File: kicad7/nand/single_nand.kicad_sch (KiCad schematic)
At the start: 14 parts, among them U1 TL074

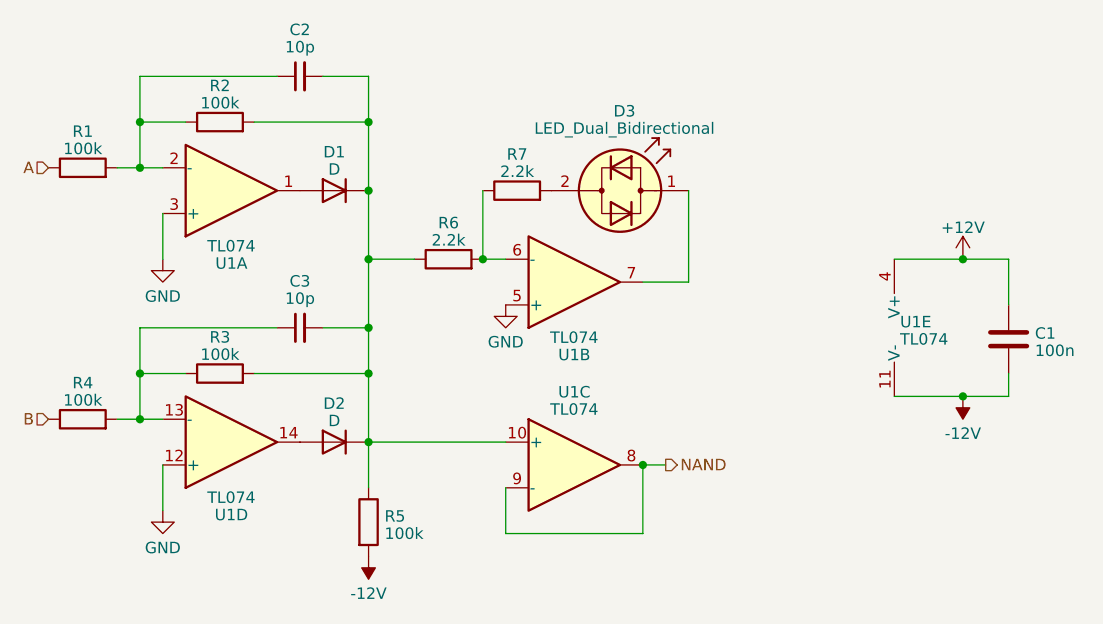
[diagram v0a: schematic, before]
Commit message: alt nand submodule layout. looking better but a lot of jumpers
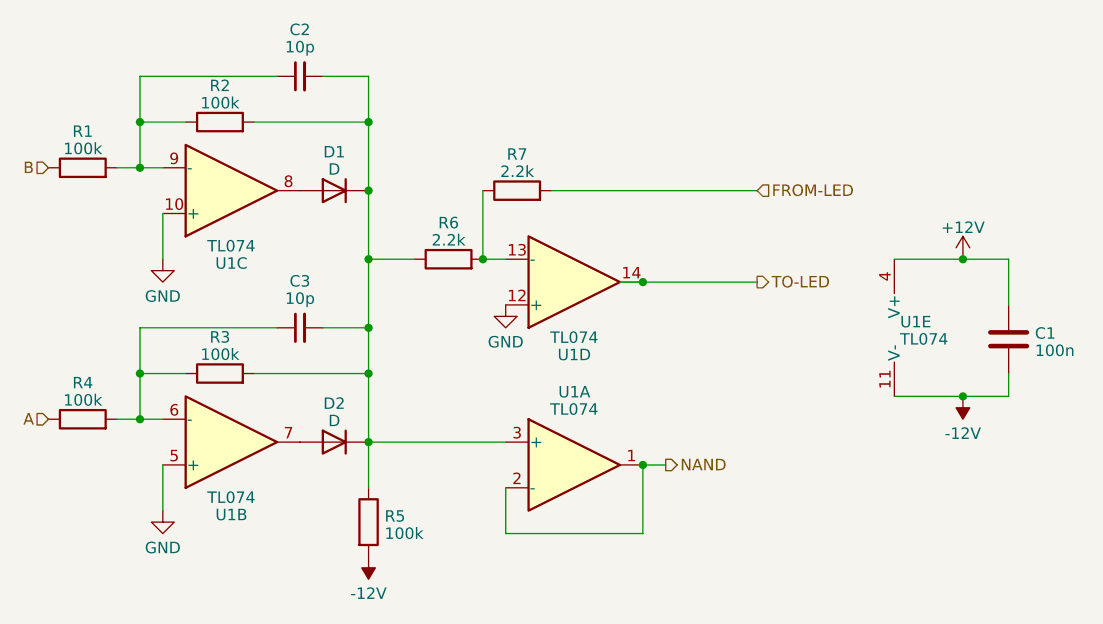
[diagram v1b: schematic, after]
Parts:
- removed D3: LED_Dual_Bidirectional, LED_THT:LED_D3.0mm, symbol Device:LED_Dual_Bidirectional
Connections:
- net A: now also R4.1; no longer R1.1
- net B: now also R1.1; no longer R4.1
- net GND: now also U1.10 (+), U1.12 (+), U1.5 (+); no longer U1.12 (+), U1.3 (+), U1.5 (+)
- net NAND: now also U1.1, U1.2 (-); no longer U1.8, U1.9 (-)
- net FROM-LED: now reaches R7.2
- net at C2.1, R1.2, R2.1: now also U1.9 (-); no longer U1.2 (-)
- net at C3.1, R3.1, R4.2: now also U1.6 (-); no longer U1.13 (-)
- net at D2.2 (A): now also U1.7; no longer U1.14
- net at R6.2, R7.1: now also U1.13 (-); no longer U1.6 (-)
- net at C2.2, C3.2, D1.1 (K)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: now also U1.3 (+); no longer U1.10 (+)
- net at D1.2 (A): now also U1.8; no longer U1.1
- new net TO-LED: U1.14
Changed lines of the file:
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@@
 (kicad_sch (version 20230121) (generator eeschema)
   (paper "A4")
+  (junction (at 58.42 33.02) (diameter 0) (color 0 0 0 0)
+  )
   (junction (at 58.42 38.1) (diameter 0) (color 0 0 0 0)
   )
-  (junction (at 58.42 33.02) (diameter 0) (color 0 0 0 0)
-  )
   (junction (at 114.3 71.12) (diameter 0) (color 0 0 0 0)
   )
@@
   (junction (at 83.82 55.88) (diameter 0) (color 0 0 0 0)
   )
+  (junction (at 114.3 50.8) (diameter 0) (color 0 0 0 0)
+  )
   (junction (at 83.82 33.02) (diameter 0) (color 0 0 0 0)
   )
@@
     (stroke (width 0) (type default))
   )
+  (wire (pts (xy 99.06 78.74) (xy 99.06 73.66))
+    (stroke (width 0) (type default))
+  )
+  (wire (pts (xy 83.82 48.26) (xy 83.82 55.88))
+    (stroke (width 0) (type default))
+  )
+  (wire (pts (xy 104.14 40.64) (xy 127 40.64))
+    (stroke (width 0) (type default))
+  )
+  (wire (pts (xy 58.42 38.1) (xy 60.96 38.1))
+    (stroke (width 0) (type default))
+  )
+  (wire (pts (xy 83.82 60.96) (xy 83.82 68.58))
+    (stroke (width 0) (type default))
+  )
+  (wire (pts (xy 78.74 55.88) (xy 83.82 55.88))
+    (stroke (width 0) (type default))
+  )
+  (wire (pts (xy 55.88 66.04) (xy 58.42 66.04))
+    (stroke (width 0) (type default))
+  )
+  (wire (pts (xy 71.12 60.96) (xy 83.82 60.96))
+    (stroke (width 0) (type default))
+  )
+  (wire (pts (xy 83.82 68.58) (xy 83.82 73.66))
+    (stroke (width 0) (type default))
+  )
+  (wire (pts (xy 154.94 63.5) (xy 154.94 60.96))
+    (stroke (width 0) (type default))
+  )
+  (wire (pts (xy 78.74 27.94) (xy 83.82 27.94))
+    (stroke (width 0) (type default))
+  )
+  (wire (pts (xy 111.76 50.8) (xy 114.3 50.8))
+    (stroke (width 0) (type default))
+  )
+  (wire (pts (xy 96.52 48.26) (xy 99.06 48.26))
+    (stroke (width 0) (type default))
+  )
+  (wire (pts (xy 83.82 68.58) (xy 99.06 68.58))
+    (stroke (width 0) (type default))
+  )
+  (wire (pts (xy 73.66 55.88) (xy 58.42 55.88))
+    (stroke (width 0) (type default))
+  )
+  (wire (pts (xy 114.3 78.74) (xy 99.06 78.74))
+    (stroke (width 0) (type default))
+  )
+  (wire (pts (xy 58.42 27.94) (xy 58.42 33.02))
+    (stroke (width 0) (type default))
+  )
+  (wire (pts (xy 71.12 33.02) (xy 83.82 33.02))
+    (stroke (width 0) (type default))
+  )
+  (wire (pts (xy 83.82 55.88) (xy 83.82 60.96))
+    (stroke (width 0) (type default))
+  )
+  (wire (pts (xy 83.82 48.26) (xy 88.9 48.26))
+    (stroke (width 0) (type default))
+  )
+  (wire (pts (xy 58.42 66.04) (xy 60.96 66.04))
+    (stroke (width 0) (type default))
+  )
+  (wire (pts (xy 58.42 60.96) (xy 63.5 60.96))
+    (stroke (width 0) (type default))
+  )
+  (wire (pts (xy 58.42 55.88) (xy 58.42 60.96))
+    (stroke (width 0) (type default))
+  )
+  (wire (pts (xy 96.52 40.64) (xy 96.52 48.26))
+    (stroke (width 0) (type default))
+  )
+  (wire (pts (xy 60.96 43.18) (xy 60.96 48.26))
+    (stroke (width 0) (type default))
+  )
+  (wire (pts (xy 149.86 63.5) (xy 154.94 63.5))
+    (stroke (width 0) (type default))
+  )
+  (wire (pts (xy 114.3 71.12) (xy 114.3 78.74))
+    (stroke (width 0) (type default))
+  )
   (wire (pts (xy 55.88 38.1) (xy 58.42 38.1))
     (stroke (width 0) (type default))
   )
-  (wire (pts (xy 99.06 78.74) (xy 99.06 73.66))
-    (stroke (width 0) (type default))
-  )
-  (wire (pts (xy 83.82 48.26) (xy 83.82 55.88))
-    (stroke (width 0) (type default))
-  )
-  (wire (pts (xy 58.42 38.1) (xy 60.96 38.1))
-    (stroke (width 0) (type default))
-  )
-  (wire (pts (xy 83.82 60.96) (xy 83.82 68.58))
-    (stroke (width 0) (type default))
-  )
-  (wire (pts (xy 78.74 55.88) (xy 83.82 55.88))
-    (stroke (width 0) (type default))
-  )
-  (wire (pts (xy 55.88 66.04) (xy 58.42 66.04))
-    (stroke (width 0) (type default))
-  )
-  (wire (pts (xy 71.12 60.96) (xy 83.82 60.96))
-    (stroke (width 0) (type default))
-  )
-  (wire (pts (xy 83.82 68.58) (xy 83.82 73.66))
-    (stroke (width 0) (type default))
-  )
-  (wire (pts (xy 154.94 63.5) (xy 154.94 60.96))
-    (stroke (width 0) (type default))
-  )
-  (wire (pts (xy 78.74 27.94) (xy 83.82 27.94))
-    (stroke (width 0) (type default))
-  )
-  (wire (pts (xy 96.52 48.26) (xy 99.06 48.26))
-    (stroke (width 0) (type default))
-  )
-  (wire (pts (xy 119.38 50.8) (xy 119.38 40.64))
-    (stroke (width 0) (type default))
-  )
-  (wire (pts (xy 83.82 68.58) (xy 99.06 68.58))
-    (stroke (width 0) (type default))
-  )
-  (wire (pts (xy 73.66 55.88) (xy 58.42 55.88))
-    (stroke (width 0) (type default))
-  )
-  (wire (pts (xy 114.3 78.74) (xy 99.06 78.74))
-    (stroke (width 0) (type default))
-  )
-  (wire (pts (xy 58.42 27.94) (xy 58.42 33.02))
-    (stroke (width 0) (type default))
-  )
-  (wire (pts (xy 71.12 33.02) (xy 83.82 33.02))
-    (stroke (width 0) (type default))
-  )
-  (wire (pts (xy 83.82 55.88) (xy 83.82 60.96))
-    (stroke (width 0) (type default))
-  )
-  (wire (pts (xy 83.82 48.26) (xy 88.9 48.26))
-    (stroke (width 0) (type default))
-  )
-  (wire (pts (xy 58.42 66.04) (xy 60.96 66.04))
-    (stroke (width 0) (type default))
-  )
-  (wire (pts (xy 58.42 60.96) (xy 63.5 60.96))
-    (stroke (width 0) (type default))
-  )
-  (wire (pts (xy 58.42 55.88) (xy 58.42 60.96))
-    (stroke (width 0) (type default))
-  )
-  (wire (pts (xy 96.52 40.64) (xy 96.52 48.26))
-    (stroke (width 0) (type default))
-  )
-  (wire (pts (xy 60.96 43.18) (xy 60.96 48.26))
-    (stroke (width 0) (type default))
-  )
-  (wire (pts (xy 149.86 63.5) (xy 154.94 63.5))
-    (stroke (width 0) (type default))
-  )
-  (wire (pts (xy 114.3 71.12) (xy 114.3 78.74))
-    (stroke (width 0) (type default))
-  )
-  (wire (pts (xy 114.3 50.8) (xy 119.38 50.8))
-    (stroke (width 0) (type default))
-  )
   (wire (pts (xy 58.42 60.96) (xy 58.42 66.04))
     (stroke (width 0) (type default))
@@
     (stroke (width 0) (type default))
   )
+  (wire (pts (xy 114.3 50.8) (xy 127 50.8))
+    (stroke (width 0) (type default))
+  )
   (wire (pts (xy 58.42 33.02) (xy 58.42 38.1))
     (stroke (width 0) (type default))
@@
     (stroke (width 0) (type default))
   )
-  (hierarchical_label "B" (shape input) (at 48.26 66.04 180) (fields_autoplaced)
+  (hierarchical_label "TO-LED" (shape output) (at 127 50.8 0) (fields_autoplaced)
+    (effects (font (size 1.27 1.27)) (justify left))
+  )
+  (hierarchical_label "B" (shape input) (at 48.26 38.1 180) (fields_autoplaced)
     (effects (font (size 1.27 1.27)) (justify right))
   )
@@
     (effects (font (size 1.27 1.27)) (justify left))
   )
-  (hierarchical_label "A" (shape input) (at 48.26 38.1 180) (fields_autoplaced)
+  (hierarchical_label "A" (shape input) (at 48.26 66.04 180) (fields_autoplaced)
     (effects (font (size 1.27 1.27)) (justify right))
   )
-  (symbol (lib_id "Device:LED_Dual_Bidirectional") (at 111.76 40.64 0) (unit 1)
-    (in_bom yes) (on_board yes) (dnp no) (fields_autoplaced)
-    (property "Reference" "D3" (at 112.2553 31.8135 0)
-      (effects (font (size 1.27 1.27)))
-    )
-    (property "Value" "LED_Dual_Bidirectional" (at 112.2553 33.7345 0)
-      (effects (font (size 1.27 1.27)))
-    )
-    (property "Footprint" "LED_THT:LED_D3.0mm" (at 111.76 40.64 0)
-      (effects (font (size 1.27 1.27)) hide)
-    )
-    (property "Datasheet" "~" (at 111.76 40.64 0)
-      (effects (font (size 1.27 1.27)) hide)
-    )
-    (pin "1")
-    (pin "2")
-    (instances
-      (project "nand"
-        (path "/f93cbd5a-5ca8-4fa6-8951-67f1e1c8b47a/f28bb2fb-651c-4eb4-acbc-bb081a05250a"
-          (reference "D3") (unit 1)
-        )
-      )
-    )
+  (hierarchical_label "FROM-LED" (shape input) (at 127 40.64 0) (fields_autoplaced)
+    (effects (font (size 1.27 1.27)) (justify left))
   )
   (symbol (lib_id "Device:R") (at 52.07 38.1 90) (unit 1)
@@
     )
   )
-  (symbol (lib_id "Amplifier_Operational:TL074") (at 68.58 68.58 0) (mirror x) (unit 4)
+  (symbol (lib_id "Amplifier_Operational:TL074") (at 68.58 68.58 0) (mirror x) (unit 2)
     (in_bom yes) (on_board yes) (dnp no)
     (property "Reference" "U1" (at 68.58 76.6699 0)
@@
       (project "nand"
         (path "/f93cbd5a-5ca8-4fa6-8951-67f1e1c8b47a/f28bb2fb-651c-4eb4-acbc-bb081a05250a"
-          (reference "U1") (unit 4)
-        )
-      )
-    )
-  )
-  (symbol (lib_id "Amplifier_Operational:TL074") (at 106.68 50.8 0) (mirror x) (unit 2)
+          (reference "U1") (unit 2)
+        )
+      )
+    )
+  )
+  (symbol (lib_id "Amplifier_Operational:TL074") (at 106.68 50.8 0) (mirror x) (unit 4)
     (in_bom yes) (on_board yes) (dnp no)
     (property "Reference" "U1" (at 106.68 58.8899 0)
@@
       (project "nand"
         (path "/f93cbd5a-5ca8-4fa6-8951-67f1e1c8b47a/f28bb2fb-651c-4eb4-acbc-bb081a05250a"
-          (reference "U1") (unit 2)
-        )
-      )
-    )
-  )
-  (symbol (lib_id "Amplifier_Operational:TL074") (at 106.68 71.12 0) (unit 3)
+          (reference "U1") (unit 4)
+        )
+      )
+    )
+  )
+  (symbol (lib_id "Amplifier_Operational:TL074") (at 106.68 71.12 0) (unit 1)
     (in_bom yes) (on_board yes) (dnp no) (fields_autoplaced)
     (property "Reference" "U1" (at 106.68 63.0301 0)
@@
       (project "nand"
         (path "/f93cbd5a-5ca8-4fa6-8951-67f1e1c8b47a/f28bb2fb-651c-4eb4-acbc-bb081a05250a"
-          (reference "U1") (unit 3)
-        )
-      )
-    )
-  )
-  (symbol (lib_id "Amplifier_Operational:TL074") (at 68.58 40.64 0) (mirror x) (unit 1)
+          (reference "U1") (unit 1)
+        )
+      )
+    )
+  )
+  (symbol (lib_id "Amplifier_Operational:TL074") (at 68.58 40.64 0) (mirror x) (unit 3)
     (in_bom yes) (on_board yes) (dnp no)
     (property "Reference" "U1" (at 68.58 48.7299 0)
@@
       (project "nand"
         (path "/f93cbd5a-5ca8-4fa6-8951-67f1e1c8b47a/f28bb2fb-651c-4eb4-acbc-bb081a05250a"
-          (reference "U1") (unit 1)
-        )
-      )
+          (reference "U1") (unit 3)
+        )
+      )
